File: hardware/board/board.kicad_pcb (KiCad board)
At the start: 2 copper layers, 20 x 108 mm, 66 parts, among them J1 Power, J10 OUT B3, J12 IN C, J13 OUT C1, J14 OUT C2, J15 OUT C3, J17 OUT D, J18 IN D1, J19 IN D2, J2 IN A, J20 IN D3, J3 OUT A1, J4 OUT A2, J5 OUT A3, J7 IN B, J8 OUT B1, J9 OUT B2, U1 OPA4991, U2 OPA4991, U4 OPA4991, U6 OPA4991

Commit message: Update values for resistors
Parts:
- R1, R12, R13, R14, R2, R3, R5, R6, R7: value 100R -> 50R
- R10, R11, R16, R9: value 270R -> 1.5k

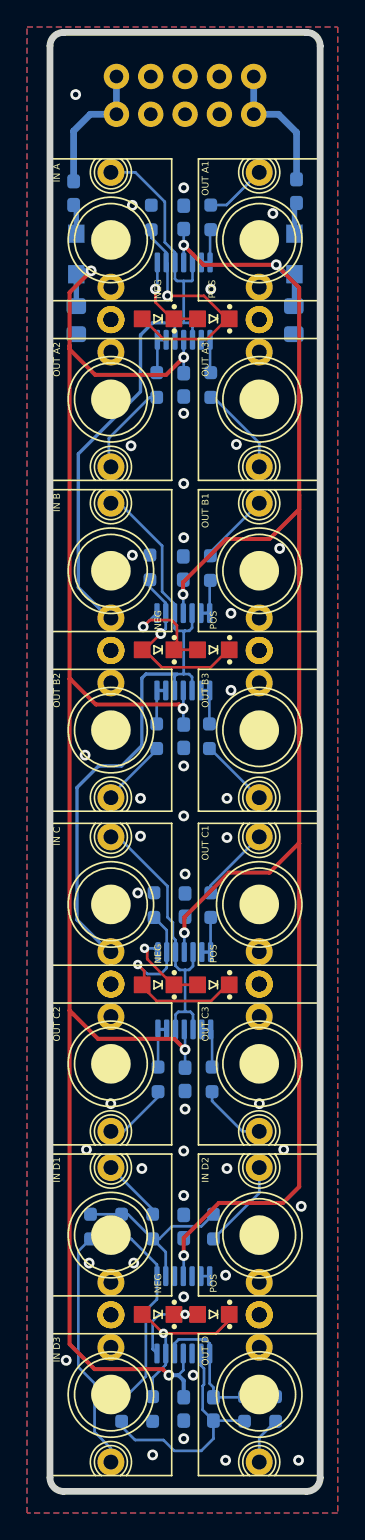
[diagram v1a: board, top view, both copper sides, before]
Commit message: hardware: convert to KiCAD 6, fix C2
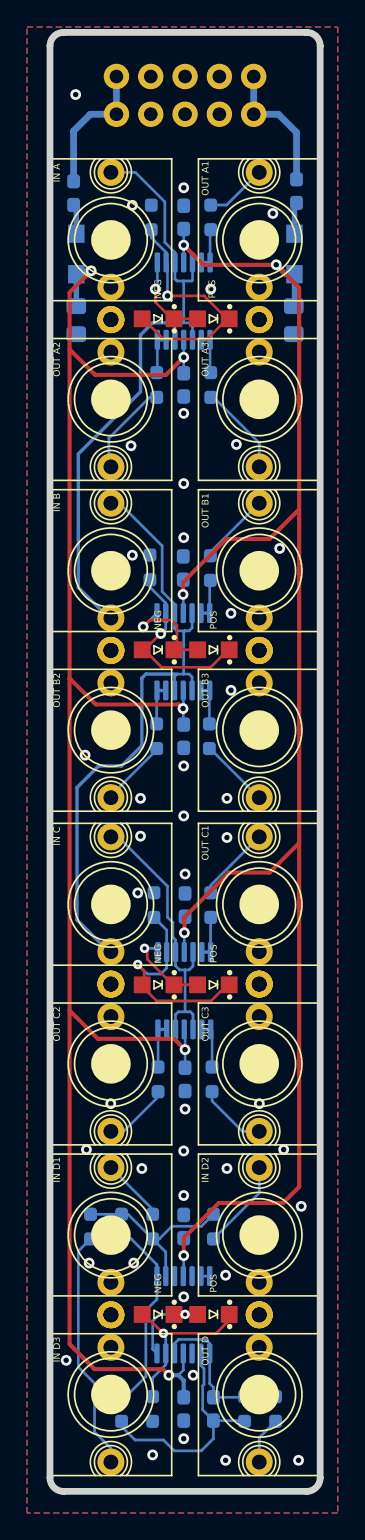
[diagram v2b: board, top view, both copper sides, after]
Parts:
- moved REF** 0.29 mm to (99.3, 81.0)
- turned C2 to 90 degrees
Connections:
- C2 pad 1: -12V -> GND
- C2 pad 2: GND -> -12V
- J10 pad TN: Net-(J10-PadTN) -> unconnected-(J10-PadTN)
- J13 pad TN: Net-(J13-PadTN) -> unconnected-(J13-PadTN)
- J14 pad TN: Net-(J14-PadTN) -> unconnected-(J14-PadTN)
- J15 pad TN: Net-(J15-PadTN) -> unconnected-(J15-PadTN)
- J17 pad TN: Net-(J17-PadTN) -> unconnected-(J17-PadTN)
- J3 pad TN: Net-(J3-PadTN) -> unconnected-(J3-PadTN)
- J4 pad TN: Net-(J4-PadTN) -> unconnected-(J4-PadTN)
- J5 pad TN: Net-(J5-PadTN) -> unconnected-(J5-PadTN)
- J8 pad TN: Net-(J8-PadTN) -> unconnected-(J8-PadTN)
- J9 pad TN: Net-(J9-PadTN) -> unconnected-(J9-PadTN)
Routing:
- net +12V: track 127.2 -> 125.7 mm
- net -12V: track 133.2 -> 132.5 mm
- net Net-(J12-PadTN): track 47.8 -> 47.2 mm
- net Net-(D5-Pad2): track 8.35 -> 7.79 mm
- net Net-(D3-Pad1): track 18.3 -> 17.7 mm
- net Net-(J12-PadT): track 21.2 -> 20.6 mm
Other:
- net class 12V removed
- net class 3.3V removed
- net class Absolute minimum removed
- net class Analog removed
- net class Default removed
